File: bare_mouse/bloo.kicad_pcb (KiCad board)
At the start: 2 copper layers, 100 x 105.9 mm, 103 parts, among them J1 Serial Debug Header, J10 Conn_01x06_Female, J2 SWD Header, J4 Conn_ARM_JTAG_SWD_10, J5 SWD Header, M1 M1_Conn_Alt, M2 M2_Conn_Alt, Q0 TEFT4300, Q1 TEFT4300, Q10 Q_NMOS_GSD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

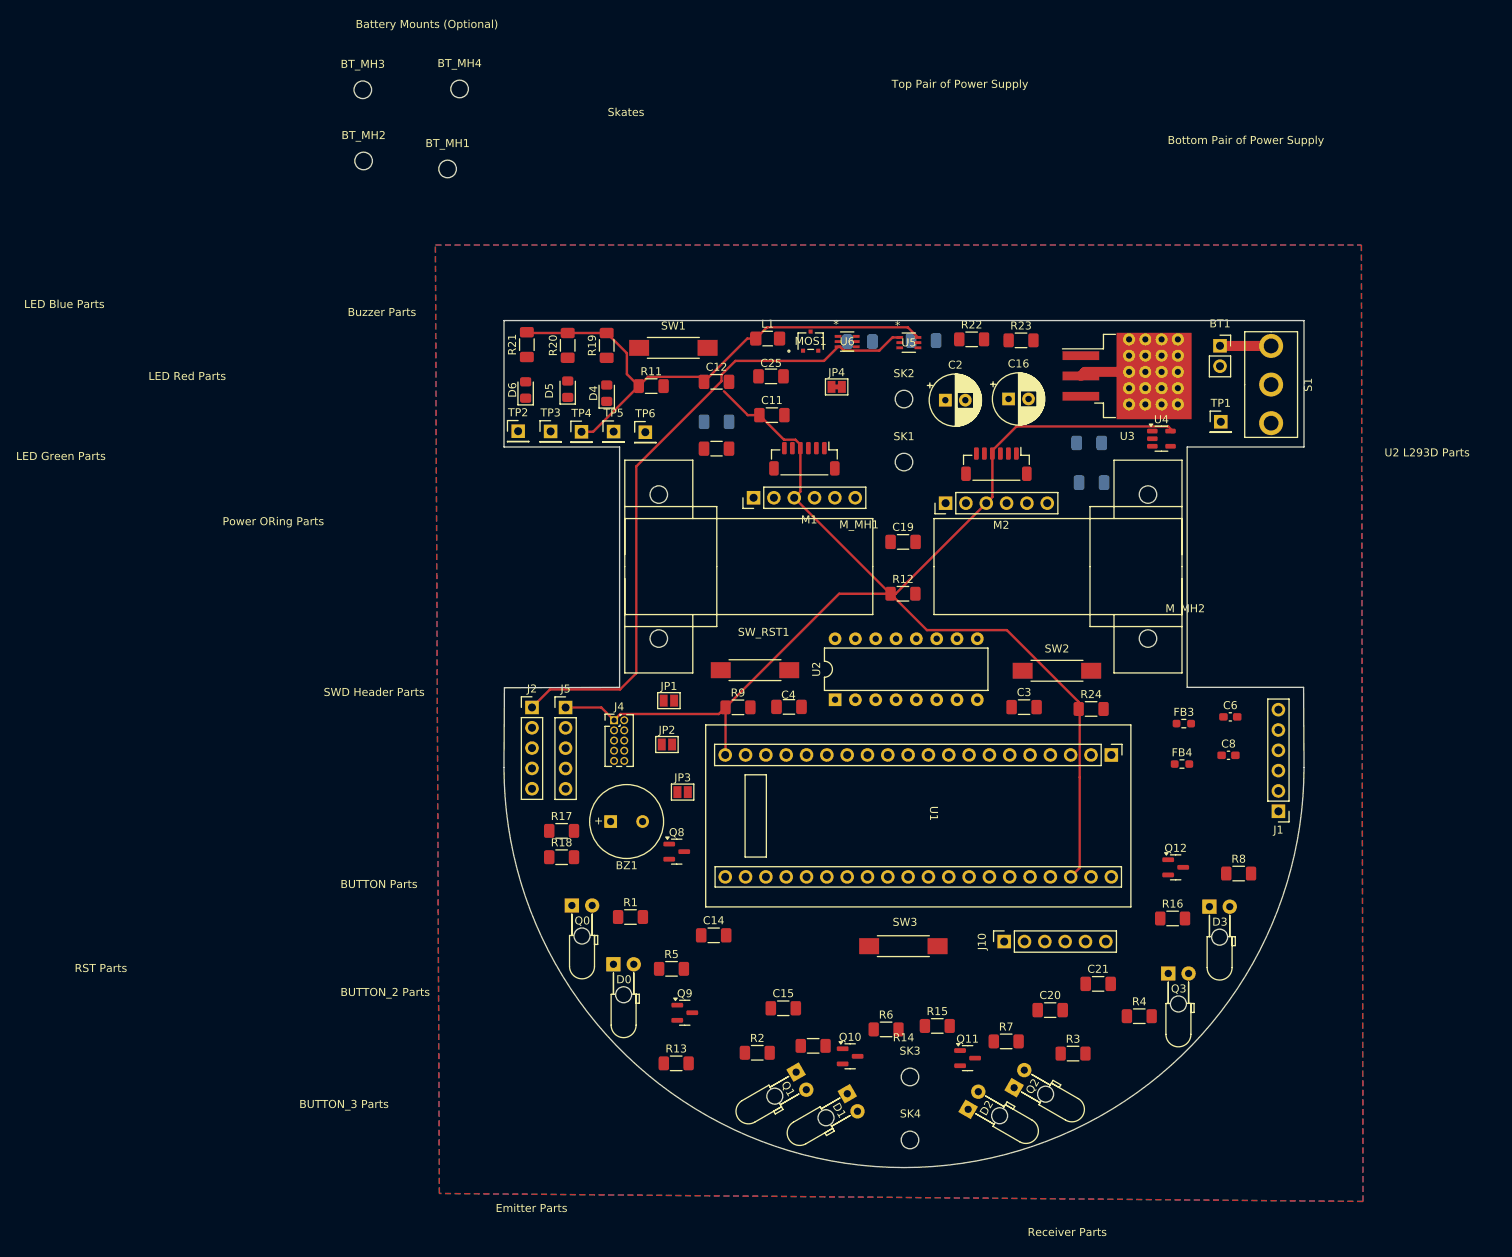
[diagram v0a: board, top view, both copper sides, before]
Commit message: moved capacitors to back
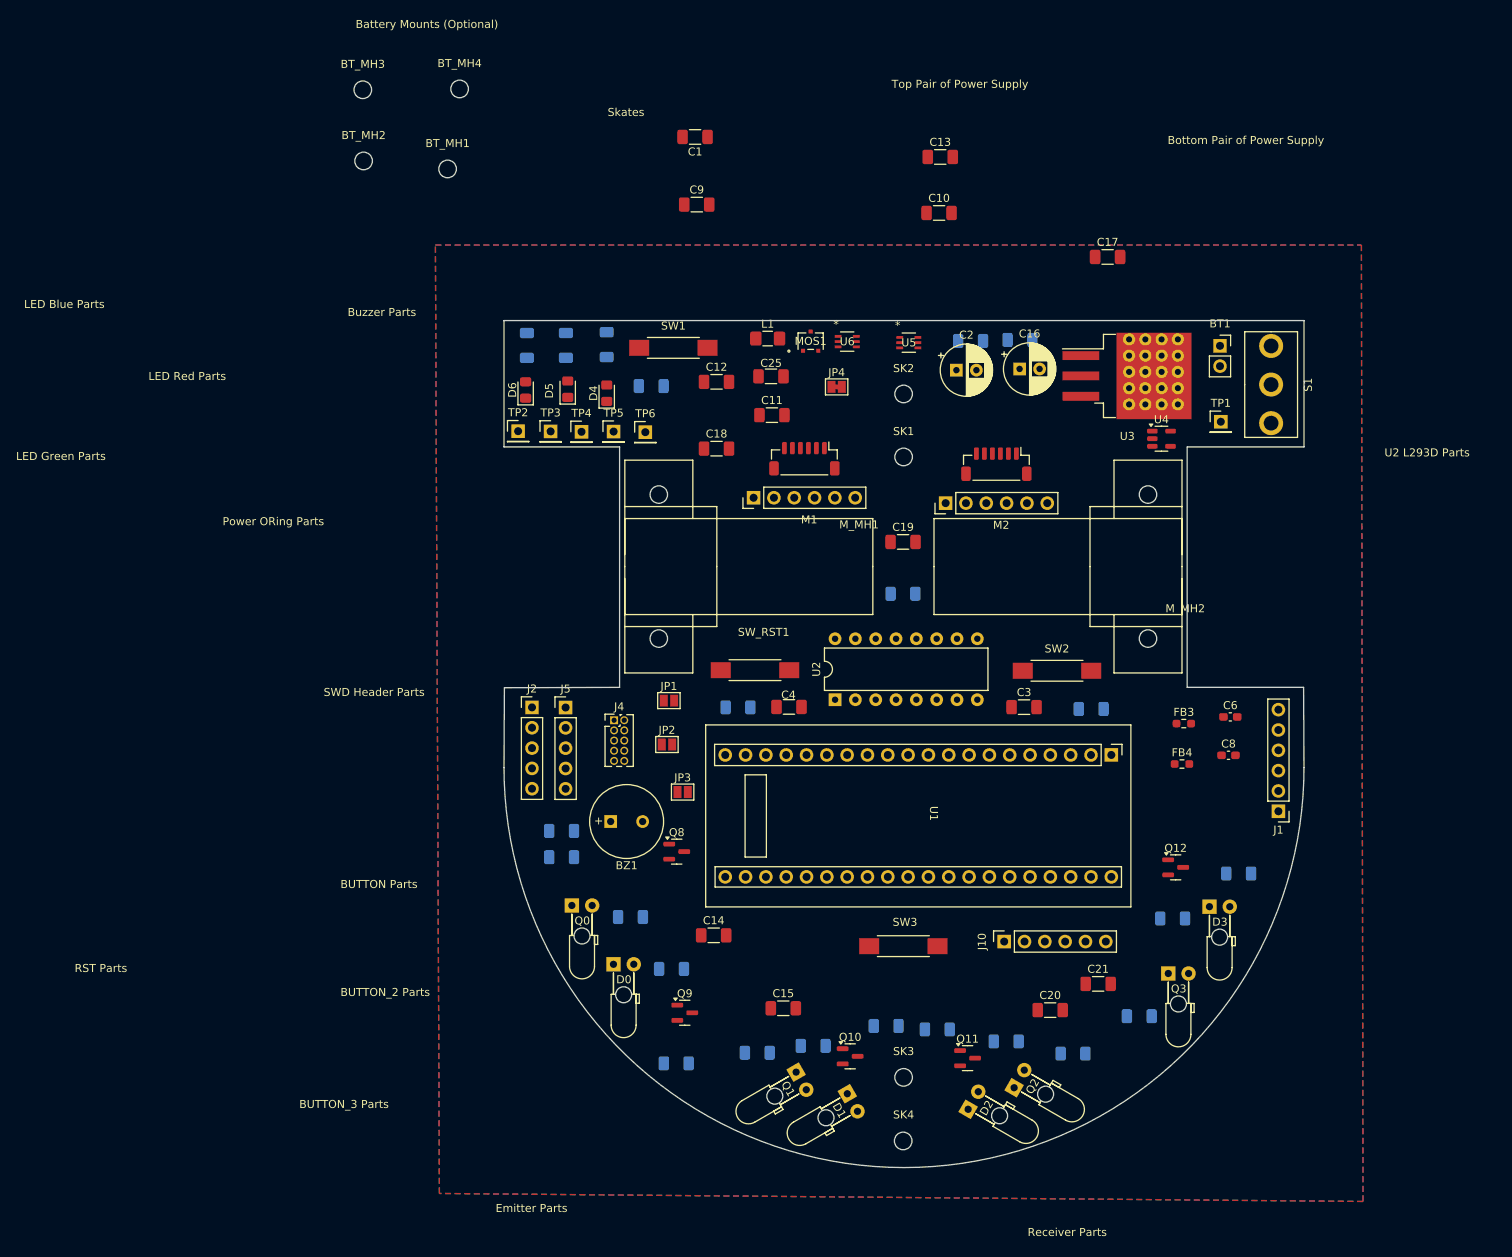
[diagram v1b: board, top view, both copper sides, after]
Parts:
- C1, C10, C13, C17, C9: moved to F.Cu
- R1, R11, R12, R13, R14, R15, R16, R17, R18, R19, R2, R20, R21, R22, R23, R24, R3, R4, R5, R6, R7, R8, R9: moved to B.Cu
- moved C1 62.4 mm to (211.9, 82.5)
- moved C9 60.4 mm to (212.1, 91.0), turned to 0 degrees
- moved C17 53.1 mm to (263.5, 97.5), turned to 0 degrees
- moved C13 23.0 mm to (242.6, 85.0), turned to 0 degrees
- moved C10 18.9 mm to (242.4, 92.0), turned to 0 degrees
- moved R19 9.98 mm to (190.9, 108.6)
- moved R21 9.98 mm to (200.9, 108.5)
- moved R15 6.40 mm to (235.8, 193.6), turned to 180 degrees
- moved R6 6.40 mm to (242.2, 194.1), turned to 180 degrees
- moved R23 6.30 mm to (246.4, 108.0), turned to 180 degrees
- moved R22 6.04 mm to (252.6, 107.9), turned to 180 degrees
- moved C16 4.00 mm to (252.5, 111.5)
- moved C2 4.00 mm to (244.6, 111.7)
- moved SK4 0.86 mm to (238.0, 207.9)
- moved SK3 0.80 mm to (238.0, 200.0)
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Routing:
- net +3V3: track 256.6 -> 0.00 mm
- net +3V3_NET: track 81.1 -> 0.00 mm
- net Net-(BT1-+): track 6.42 -> 0.00 mm
- net +5V_NET: track 6.24 -> 0.00 mm

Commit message: mira's revisions
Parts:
- moved SW3 75.4 mm to (210.2, 113.5)
- moved SW2 69.8 mm to (194.5, 118.5)
- moved C1 60.2 mm to (259.0, 120.0), turned to 90 degrees
- moved C9 58.6 mm to (263.0, 120.0), turned to -90 degrees
- moved C17 52.6 mm to (212.1, 108.7), turned to 90 degrees
- moved U4 51.8 mm to (219.8, 108.3)
- moved C13 45.1 mm to (271.0, 120.0), turned to -90 degrees
- moved BZ1 39.2 mm to (237.0, 184.5)
- moved Q8 38.9 mm to (246.4, 184.6)
- moved R17 38.9 mm to (232.0, 182.0)
- moved R18 38.9 mm to (232.0, 185.2)
- moved C10 37.2 mm to (267.0, 120.0), turned to -90 degrees
- moved JP4 34.5 mm to (261.9, 126.0)
- moved J10 34.2 mm to (280.5, 166.6), turned to 180 degrees
- moved D6 33.7 mm to (224.5, 114.9)
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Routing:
- net BATT_NET: track 0.00 -> 58.1 mm
- net +5V_NET: track 0.00 -> 35.0 mm
- net Net-(BT1-+): track 0.00 -> 6.40 mm
- net Net-(S1-Pad3): track 0.00 -> 6.36 mm
